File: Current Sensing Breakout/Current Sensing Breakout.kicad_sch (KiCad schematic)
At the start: 6 parts, among them U1 ACS725xLCTR-20AB

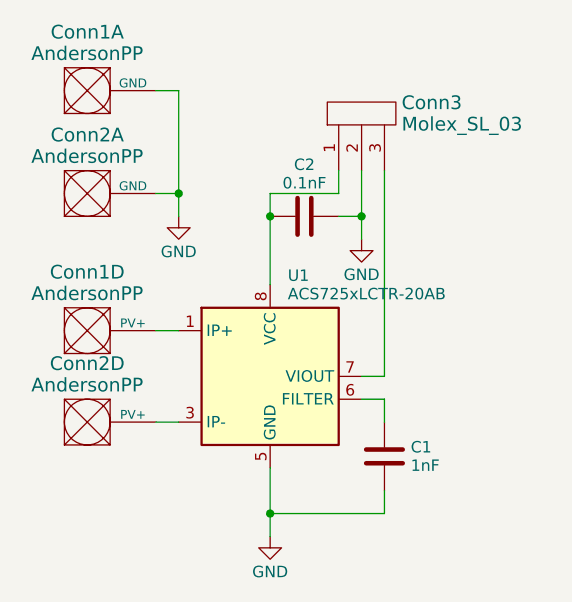
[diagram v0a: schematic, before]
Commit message: Fixed Capacitance Value
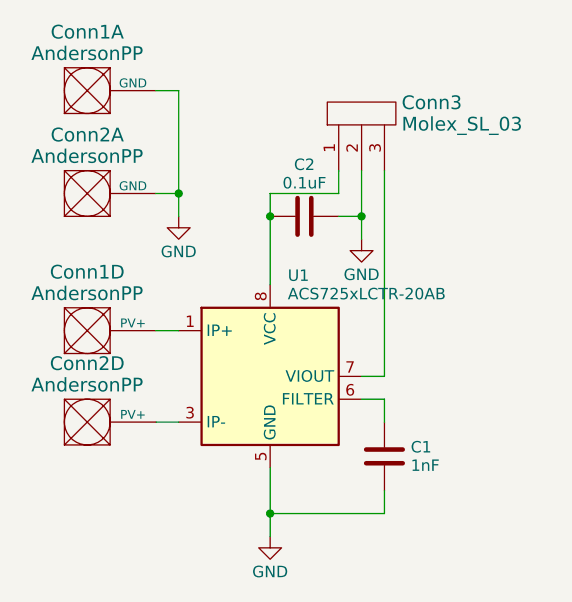
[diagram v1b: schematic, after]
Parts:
- C2: value 0.1nF -> 0.1uF
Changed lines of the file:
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@@
       (effects (font (size 1.27 1.27)))
     )
-    (property "Value" "0.1nF" (at 44.45 31.869 90)
+    (property "Value" "0.1uF" (at 44.45 31.869 90)
       (effects (font (size 1.27 1.27)))
     )
